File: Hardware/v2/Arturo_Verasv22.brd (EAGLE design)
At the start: 100 x 80 mm, 23 parts, among them T1 2SC1815, T3 2SC1815, T4 2SC1815, T5 2SC1815, T6 2SC1815, T7 2SC1815, T8 2SC1815, X1 22-23-2071

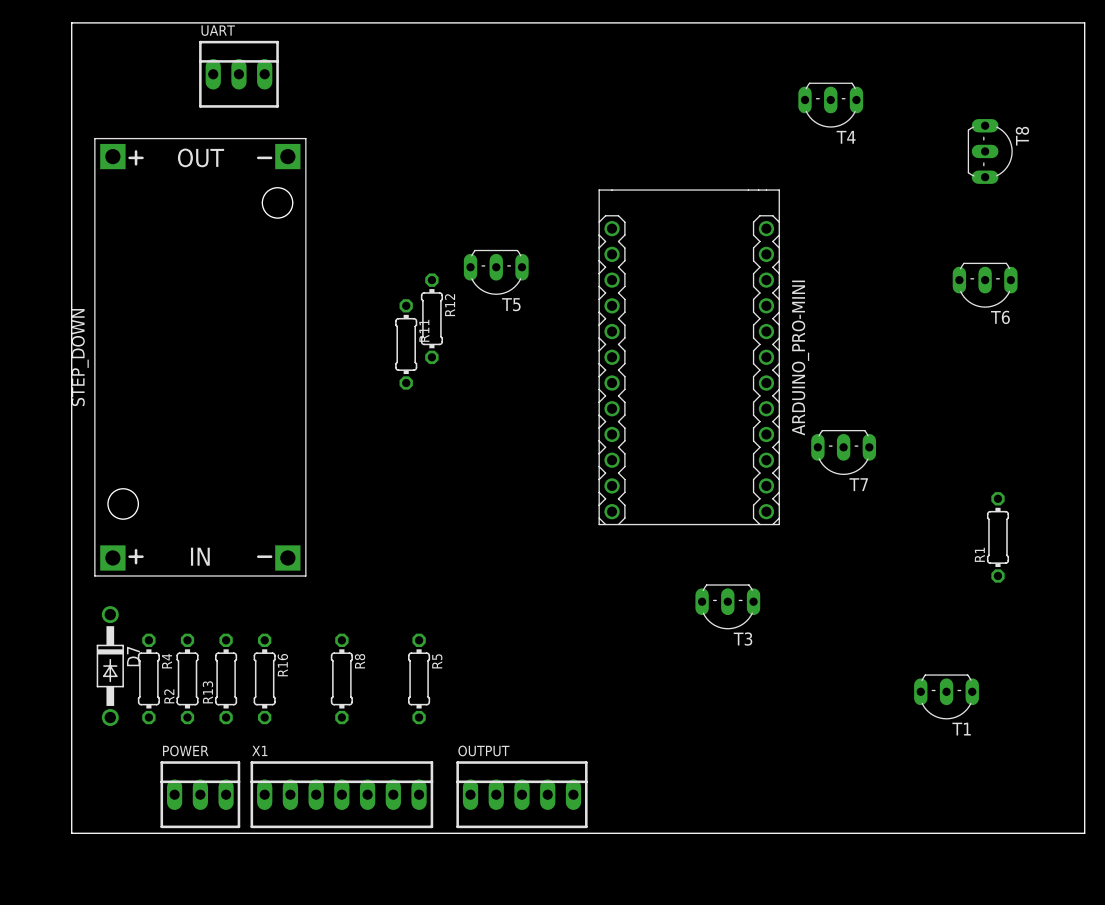
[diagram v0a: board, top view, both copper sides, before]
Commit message: Esquematico
se hace más simple el esquemático
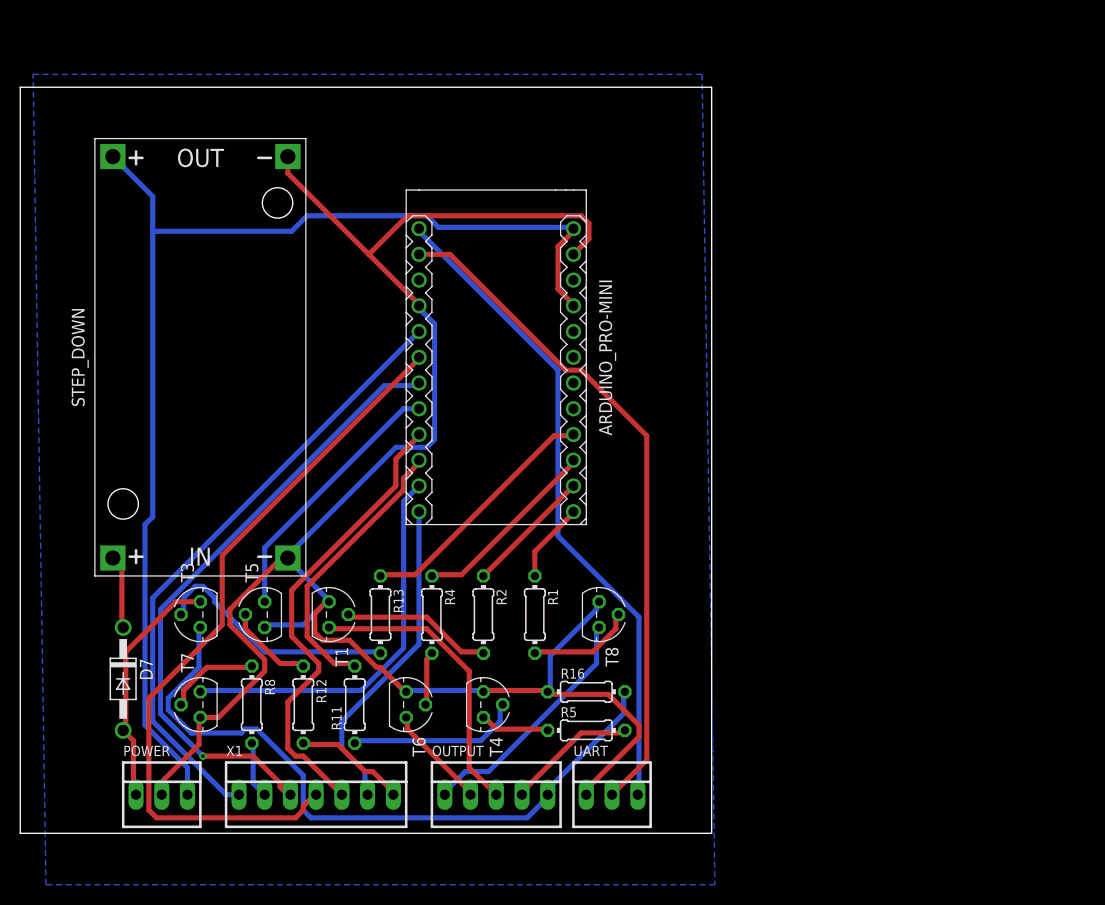
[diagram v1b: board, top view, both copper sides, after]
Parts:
- T1, T3, T4, T5, T6, T7, T8: value 2SC1815 -> 2N3904; device transistor:TO92-ECB -> transistor:TO92
- moved UART 80.1 mm to (53.3, 3.81)
- moved T6 70.9 mm to (33.0, 12.7), turned to 270 degrees
- moved T4 68.8 mm to (40.6, 12.7), turned to 270 degrees
- moved T7 68.4 mm to (12.7, 12.7), turned to 90 degrees
- moved T1 61.4 mm to (25.4, 21.6), turned to 270 degrees
- moved T8 59.5 mm to (52.1, 21.6)
- moved T3 52.1 mm to (12.7, 21.6), turned to 90 degrees
- moved R1 46.4 mm to (45.7, 21.6), turned to 270 degrees
- moved T5 41.2 mm to (19.1, 21.6), turned to 90 degrees
- moved R12 40.2 mm to (22.9, 12.7)
- moved R11 35.9 mm to (27.9, 12.7), turned to 90 degrees
- moved R16 31.8 mm to (50.8, 14.0), turned to 0 degrees
- moved R2 29.9 mm to (40.6, 21.6), turned to 270 degrees
- moved R4 28.7 mm to (35.6, 21.6)
- moved ARDUINO_PRO-MINI 19.1 mm to (41.9, 47.0)
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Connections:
- removed net N$9: ARDUINO_PRO-MINI.J7.9, UART.1
- removed net VCC: ARDUINO_PRO-MINI.J6.4, POWER.3
- net BUZZER_OUTPUT-: now also T6.1; no longer T6.C
- net CC_OUTPUT-: now also T8.1; no longer T8.C
- net DGENERAL_INPUT: now also T5.1; no longer T5.C
- net DIGNITION_INPUT: now also T7.1; no longer T7.C
- net GND: now also ARDUINO_PRO-MINI.J7.9, T1.3, T4.3, T5.3, T6.3, T7.3, T8.3, UART.1; no longer T1.E, T4.E, T5.E, T6.E, T7.E, T8.E
- net N$1: now also T5.2; no longer T5.B
- net N$2: now also T3.2; no longer T3.B
- net N$20: now also T4.2; no longer T4.B
- net N$22: now also T7.2; no longer T7.B
- net N$3: now also T8.2; no longer T8.B
- net N$4: now also T1.2; no longer T1.B
- net N$5: now also T6.2; no longer T6.B
- net N$6: now also T4.1; no longer T4.C
- net SPEAKER_OUTPUT-: now also T1.1; no longer T1.C
- net TDIN2_OUTPUT+: now also T3.3; no longer T3.E
- net VIN: now also T3.1; no longer T3.C
- net VOUT: now also ARDUINO_PRO-MINI.J6.4, POWER.3
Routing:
- net GND: track 0.00 -> 187.6 mm
- net VOUT: track 0.00 -> 118.3 mm
- net DJAMMINGAUX_INPUT-: track 0.00 -> 73.7 mm
- net TDIN2_OUTPUT+: track 0.00 -> 68.3 mm
- net N$8: track 0.00 -> 66.7 mm
- net N$7: track 0.00 -> 65.0 mm
- net DTDOUT1_INPUT-: track 0.00 -> 61.6 mm, vias 0 -> 1
- net DTDOUT2_INPUT-: track 0.00 -> 60.9 mm
- net DENABLEDOOR_INPUT-: track 0.00 -> 45.8 mm
- net DIGNITION_INPUT: track 0.00 -> 38.5 mm
- net DDOOR_INPUT-: track 0.00 -> 32.3 mm
- net SPEAKER_OUTPUT-: track 0.00 -> 28.9 mm
- net DLED_OUTPUT: track 0.00 -> 27.9 mm
- net DGENERAL_INPUT: track 0.00 -> 26.3 mm
- net DTDIN2_OUT-: track 0.00 -> 25.0 mm
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- added copper zone on layer 16, net N$9
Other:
- board size 100 x 80 mm -> 68.2 x 73.7 mm
